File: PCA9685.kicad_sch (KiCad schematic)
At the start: 24 parts, among them J10 HEADER, J11 HEADER, J12 HEADER, J13 HEADER, J14 HEADER, J15 HEADER, J7 HEADER, J8 HEADER, J9 HEADER, U1 PCA9685PW_118

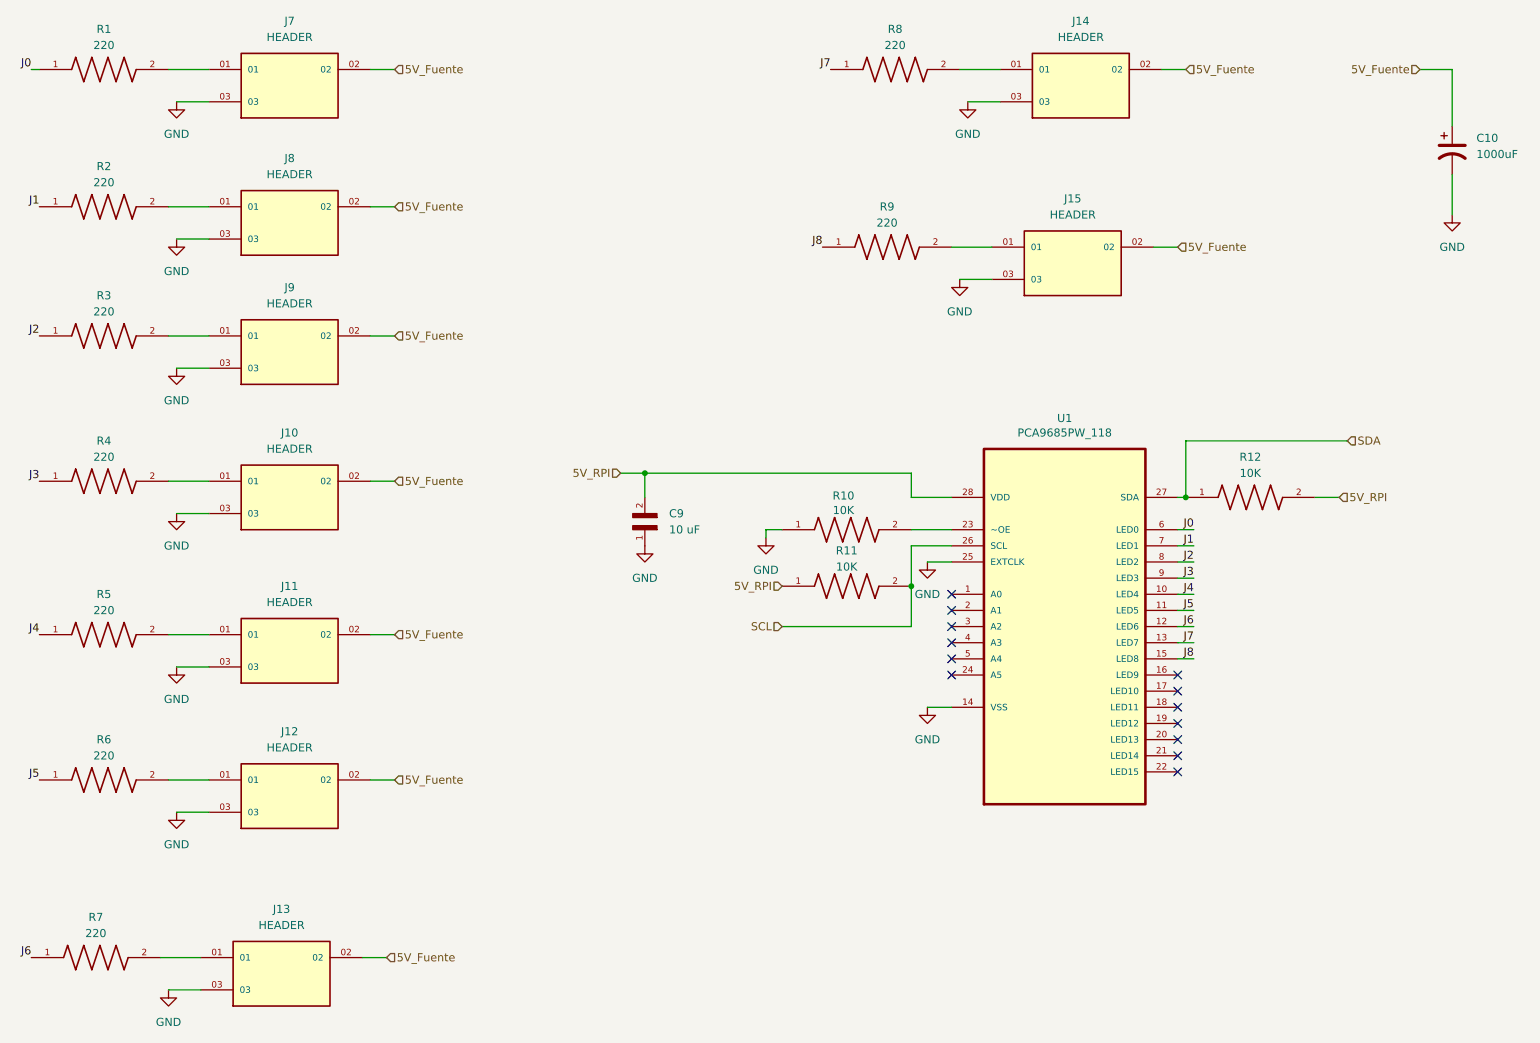
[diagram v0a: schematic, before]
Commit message: Se arranca un nuevo diseno. Se saco el regulador y 4 servos. Hay que reajustar el diseno del PCB.
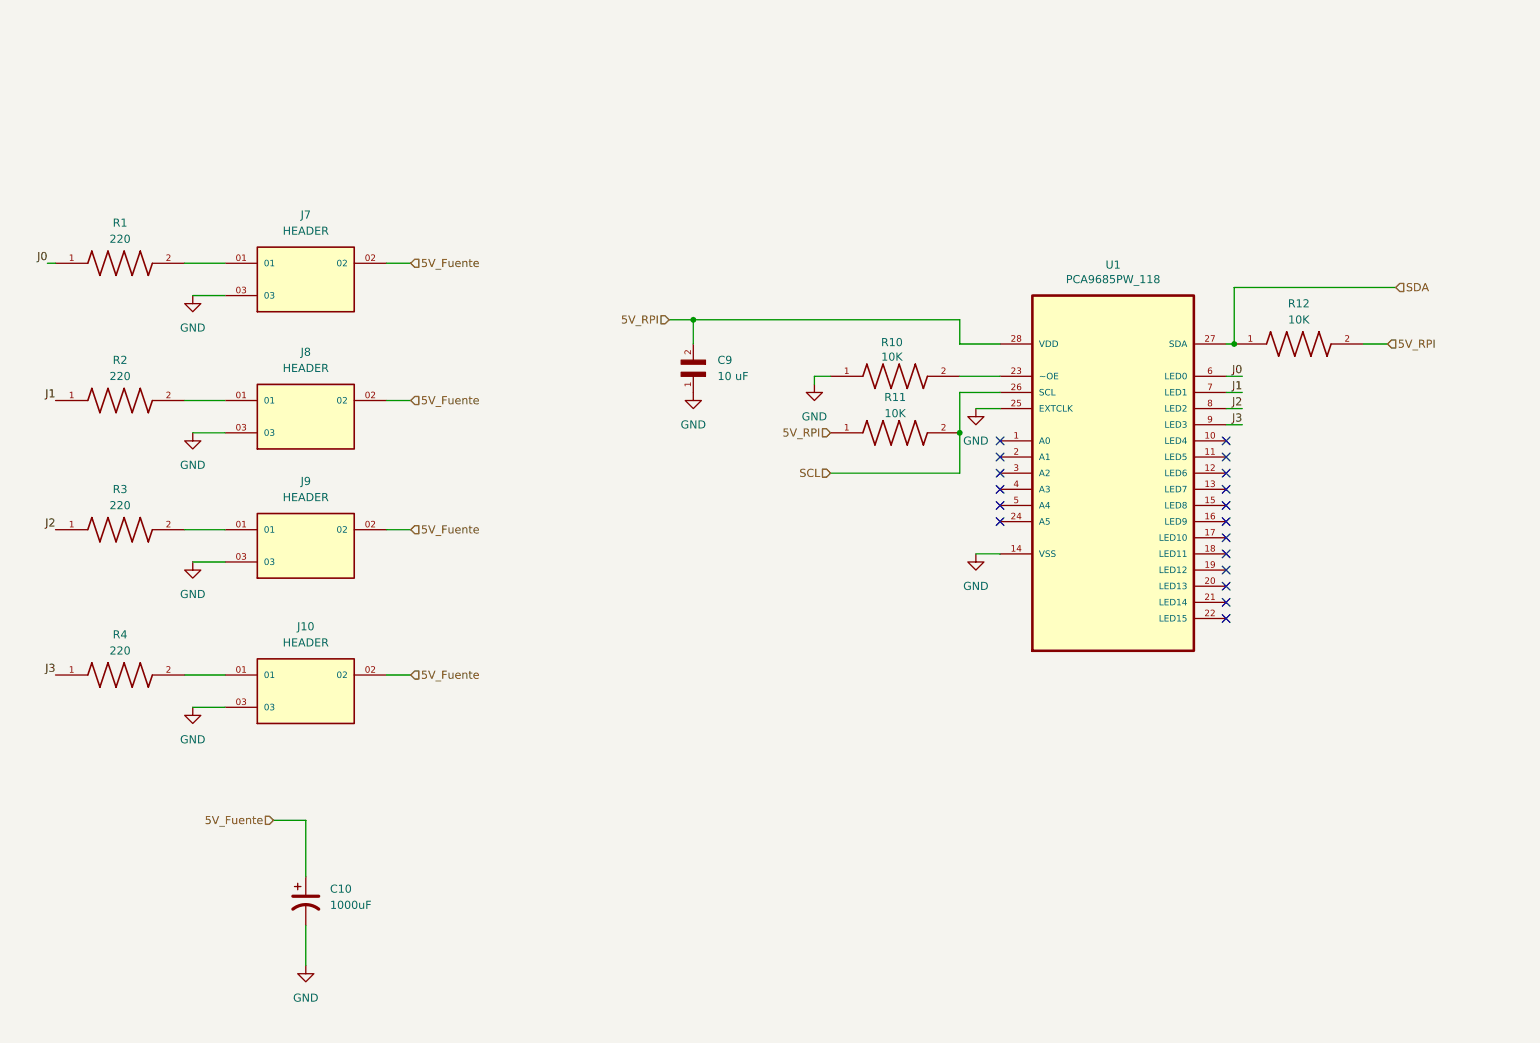
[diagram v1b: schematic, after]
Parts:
- removed J11, J12, J13, J14, J15: HEADER, TSW-101-07-T-T:SAMTEC_TSW-101-07-T-T, symbol TSW-101-07-T-T:TSW-101-07-T-T
- removed R5, R6, R7, R8, R9: 220, RC0402FR-07220RL:RESC1005X40N, symbol RC0402FR-07220RL:RC0402FR-07220RL
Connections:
- net J4: no longer names the net of U1.10 (LED4)
- net J5: no longer names the net of U1.11 (LED5)
- net J6: no longer names the net of U1.12 (LED6)
- net J7: no longer names the net of U1.13 (LED7)
- net J8: no longer names the net of U1.15 (LED8)
- no-connect marks 13 -> 18
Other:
- moved on the sheet: C10, C9, J10, J7, J8, J9, R1, R10, R11, R12, R2, R3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

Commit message: Se borro todo y se arranco de nuevo. Placa circular.
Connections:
- net 5V_Fuente is gone; now on net 5V_RPI: C10.1, J10.02, J7.02, J8.02, J9.02
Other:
- moved on the sheet: C10, C9
